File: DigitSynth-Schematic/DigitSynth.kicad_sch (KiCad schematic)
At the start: 0 parts

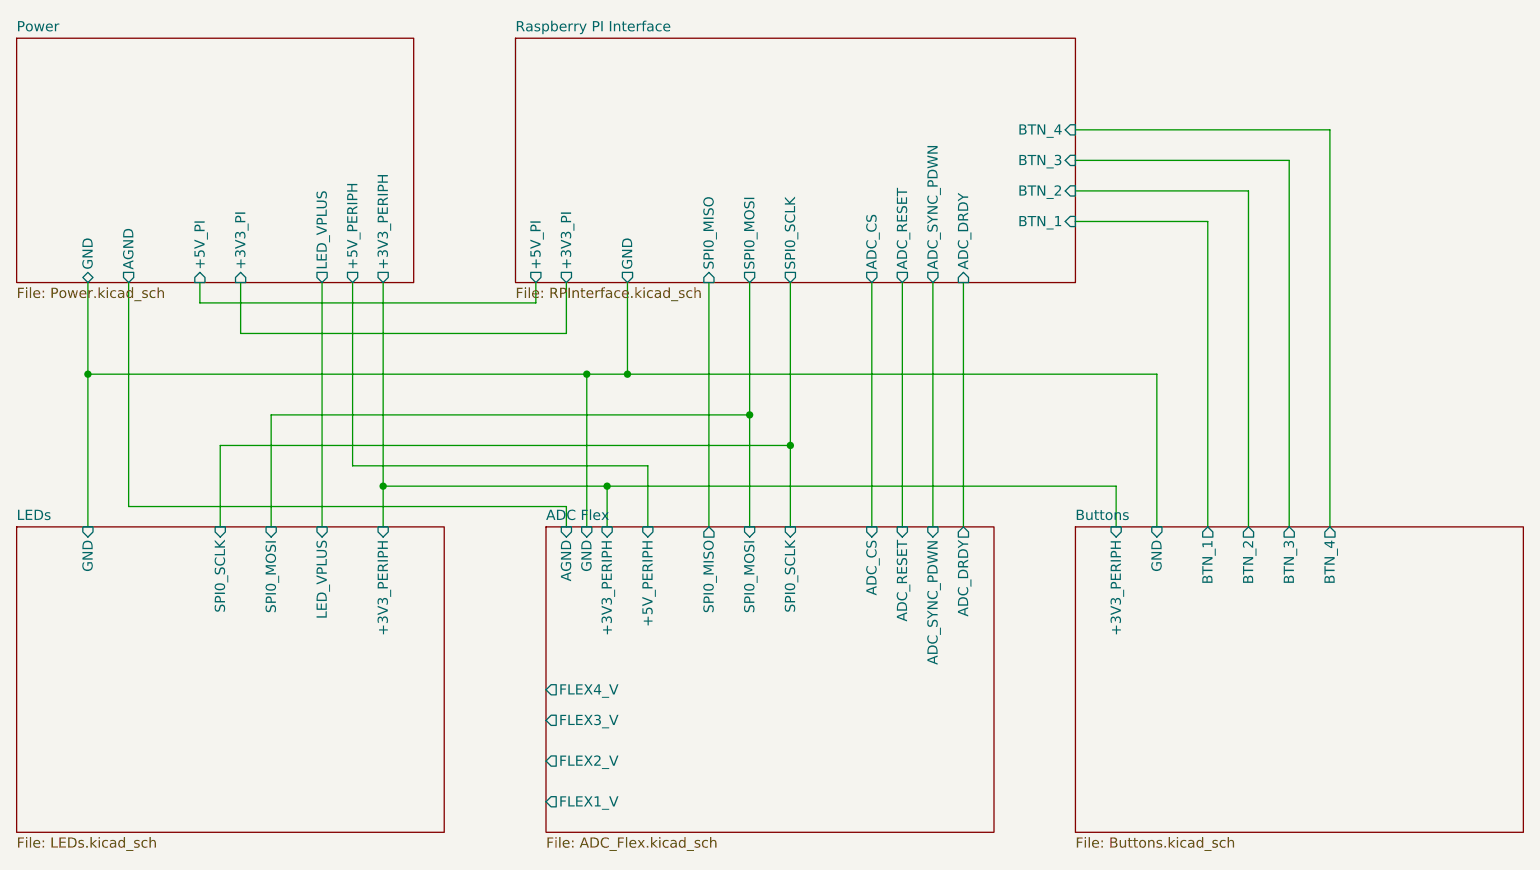
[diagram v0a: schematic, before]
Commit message: removed power schematic sheet as RPI5 has decoupling capacitors; fixed component value errors; buttons removed from RPI5 sheet and added to ADC analog inputs; LED_VPLUS power line removed and replaced by +5V_PERIPH
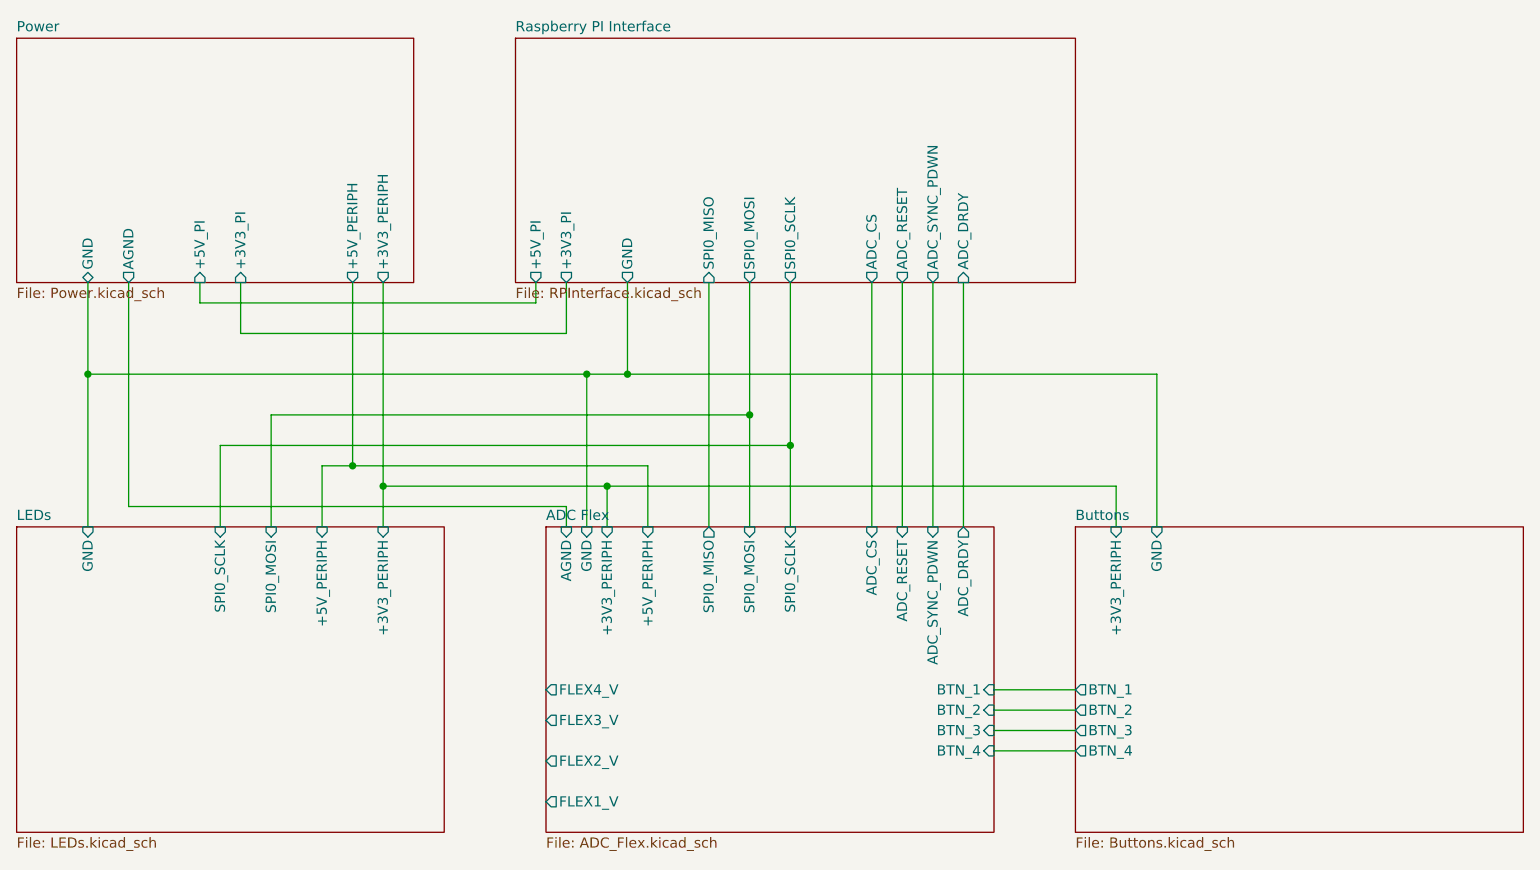
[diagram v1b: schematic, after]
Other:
- sheet ADC Flex ports: added BTN_1, BTN_2, BTN_3, BTN_4; removed none
- sheet LEDs ports: added +5V_PERIPH; removed LED_VPLUS
- sheet Power ports: added none; removed LED_VPLUS
- sheet Raspberry PI Interface ports: added none; removed BTN_1, BTN_2, BTN_3, BTN_4
- title: (none) -> DigitSynth Schematic
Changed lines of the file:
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@@
 	(generator_version "9.0")
 	(paper "A4")
+	(title_block
+		(title "DigitSynth Schematic")
+		(rev "2")
+	)
 	(junction
 		(at 121.92 73.66)
@@
 	)
 	(junction
+		(at 67.31 76.2)
+		(diameter 0)
+		(color 0 0 0 0)
+	)
+	(junction
 		(at 34.29 64.77)
 		(diameter 0)
@@
 	(wire
 		(pts
-			(xy 179.07 41.91) (xy 157.48 41.91)
+			(xy 147.32 109.22) (xy 157.48 109.22)
 		)
 		(stroke
@@
 	(wire
 		(pts
-			(xy 184.15 83.82) (xy 184.15 38.1)
+			(xy 147.32 106.68) (xy 157.48 106.68)
+		)
+		(stroke
+			(width 0)
+			(type default)
+		)
+	)
+	(wire
+		(pts
+			(xy 147.32 104.14) (xy 157.48 104.14)
 		)
 		(stroke
@@
 	(wire
 		(pts
-			(xy 63.5 53.34) (xy 63.5 83.82)
-		)
-		(stroke
-			(width 0)
-			(type default)
-		)
-	)
-	(wire
-		(pts
-			(xy 173.99 45.72) (xy 173.99 83.82)
-		)
-		(stroke
-			(width 0)
-			(type default)
-		)
-	)
-	(wire
-		(pts
-			(xy 179.07 83.82) (xy 179.07 41.91)
-		)
-		(stroke
-			(width 0)
-			(type default)
-		)
-	)
-	(wire
-		(pts
 			(xy 167.64 83.82) (xy 167.64 64.77)
 		)
@@
 	(wire
 		(pts
+			(xy 63.5 83.82) (xy 63.5 76.2)
+		)
+		(stroke
+			(width 0)
+			(type default)
+		)
+	)
+	(wire
+		(pts
 			(xy 71.12 78.74) (xy 99.06 78.74)
 		)
@@
 	(wire
 		(pts
-			(xy 189.23 34.29) (xy 157.48 34.29)
-		)
-		(stroke
-			(width 0)
-			(type default)
-		)
-	)
-	(wire
-		(pts
 			(xy 34.29 64.77) (xy 34.29 83.82)
 		)
@@
 	(wire
 		(pts
-			(xy 184.15 38.1) (xy 157.48 38.1)
-		)
-		(stroke
-			(width 0)
-			(type default)
-		)
-	)
-	(wire
-		(pts
 			(xy 39.37 81.28) (xy 93.98 81.28)
 		)
@@
 	(wire
 		(pts
-			(xy 189.23 83.82) (xy 189.23 34.29)
-		)
-		(stroke
-			(width 0)
-			(type default)
-		)
-	)
-	(wire
-		(pts
 			(xy 39.37 53.34) (xy 39.37 81.28)
 		)
@@
 	(wire
 		(pts
-			(xy 157.48 45.72) (xy 173.99 45.72)
+			(xy 63.5 76.2) (xy 67.31 76.2)
+		)
+		(stroke
+			(width 0)
+			(type default)
+		)
+	)
+	(wire
+		(pts
+			(xy 147.32 111.76) (xy 157.48 111.76)
 		)
 		(stroke
@@
 			)
 		)
-		(pin "LED_VPLUS" output
-			(at 63.5 53.34 270)
-			(effects
-				(font
-					(size 1.27 1.27)
-				)
-				(justify left)
-			)
-		)
 		(instances
 			(project "DigitSynth"
@@
 			)
 		)
-		(pin "LED_VPLUS" input
+		(pin "+5V_PERIPH" input
 			(at 63.5 83.82 90)
 			(effects
@@
 			)
 		)
-		(pin "BTN_1" input
-			(at 157.48 45.72 0)
-			(effects
-				(font
-					(size 1.27 1.27)
-				)
-				(justify right)
-			)
-		)
-		(pin "BTN_2" input
-			(at 157.48 41.91 0)
-			(effects
-				(font
-					(size 1.27 1.27)
-				)
-				(justify right)
-			)
-		)
-		(pin "BTN_3" input
-			(at 157.48 38.1 0)
-			(effects
-				(font
-					(size 1.27 1.27)
-				)
-				(justify right)
-			)
-		)
-		(pin "BTN_4" input
-			(at 157.48 34.29 0)
-			(effects
-				(font
-					(size 1.27 1.27)
-				)
-				(justify right)
-			)
-		)
 		(pin "GND" output
 			(at 101.6 53.34 270)
@@
 		)
 		(pin "BTN_1" output
-			(at 173.99 83.82 90)
-			(effects
-				(font
-					(size 1.27 1.27)
-				)
-				(justify right)
+			(at 157.48 104.14 180)
+			(effects
+				(font
+					(size 1.27 1.27)
+				)
+				(justify left)
 			)
 		)
 		(pin "BTN_2" output
-			(at 179.07 83.82 90)
-			(effects
-				(font
-					(size 1.27 1.27)
-				)
-				(justify right)
+			(at 157.48 106.68 180)
+			(effects
+				(font
+					(size 1.27 1.27)
+				)
+				(justify left)
 			)
 		)
 		(pin "BTN_3" output
-			(at 184.15 83.82 90)
-			(effects
-				(font
-					(size 1.27 1.27)
-				)
-				(justify right)
+			(at 157.48 109.22 180)
+			(effects
+				(font
+					(size 1.27 1.27)
+				)
+				(justify left)
 			)
 		)
 		(pin "BTN_4" output
-			(at 189.23 83.82 90)
-			(effects
-				(font
-					(size 1.27 1.27)
-				)
-				(justify right)
+			(at 157.48 111.76 180)
+			(effects
+				(font
+					(size 1.27 1.27)
+				)
+				(justify left)
 			)
 		)
@@
 			(effects
 				(font
+					(size 1.27 1.27)
+				)
+				(justify right)
+			)
+		)
+		(pin "BTN_1" input
+			(at 147.32 104.14 0)
+			(effects
+				(font
+					(size 1.27 1.27)
+				)
+				(justify right)
+			)
+		)
+		(pin "BTN_2" input
+			(at 147.32 106.68 0)
+			(effects
+				(font
+					(size 1.27 1.27)
+				)
+				(justify right)
+			)
+		)
+		(pin "BTN_3" input
+			(at 147.32 109.22 0)
+			(effects
+				(font
+					(size 1.27 1.27)
+				)
+				(justify right)
+			)
+		)
+		(pin "BTN_4" input
+			(at 147.32 111.76 0)
+			(effects
+				(font

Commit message: updated schematic for PCB design
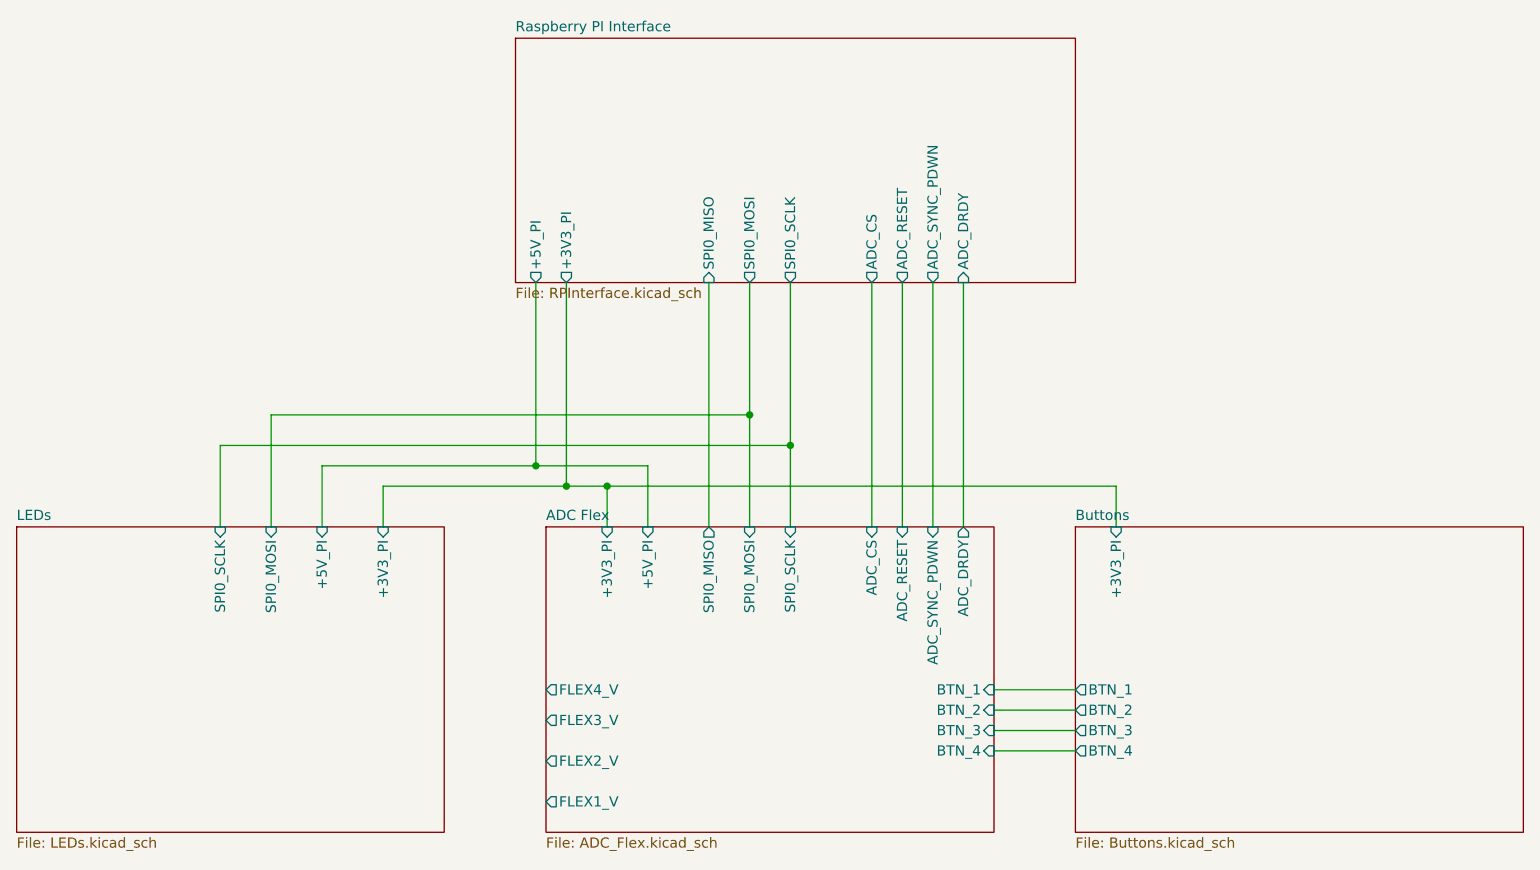
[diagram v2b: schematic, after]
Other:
- removed sheet Power
- sheet ADC Flex ports: added +3V3_PI, +5V_PI; removed +3V3_PERIPH, +5V_PERIPH, AGND, GND
- sheet Buttons ports: added +3V3_PI; removed +3V3_PERIPH, GND
- sheet LEDs ports: added +3V3_PI, +5V_PI; removed +3V3_PERIPH, +5V_PERIPH, GND
- sheet Raspberry PI Interface ports: added none; removed GND
